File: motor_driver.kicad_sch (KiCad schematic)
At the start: 30 parts, among them J1 Motor_1_Conn, J11 Motor_2_Conn, J12 Motor_4_Conn, J14 Motor_5_Conn, J4 Motor_3_Conn, Q1 NMOS, Q2 NMOS, Q3 NMOS, Q4 NMOS, Q5 NMOS

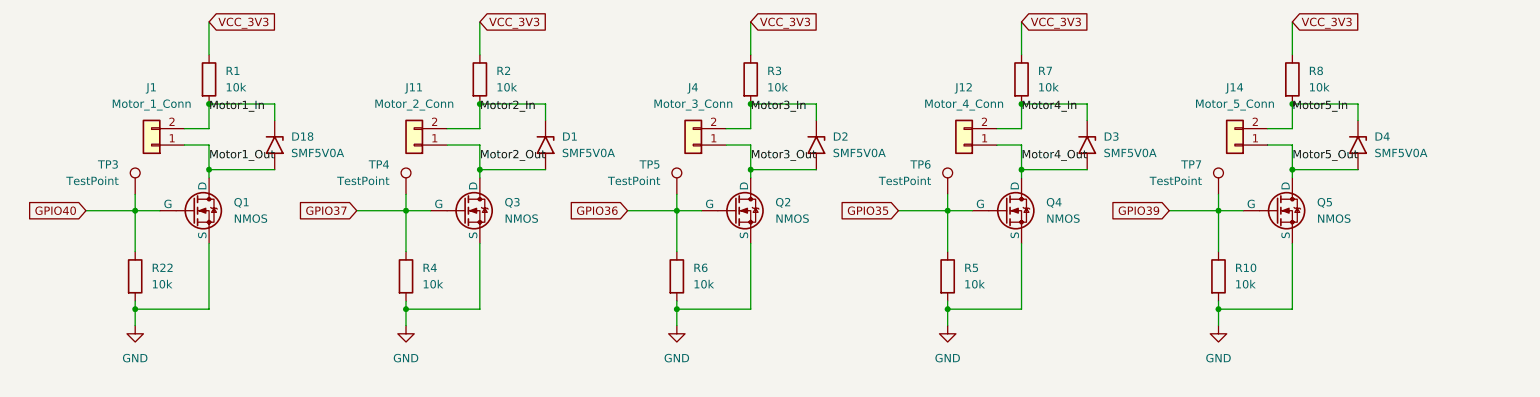
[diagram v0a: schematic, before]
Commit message: after connor fixed footprints and billy started layout
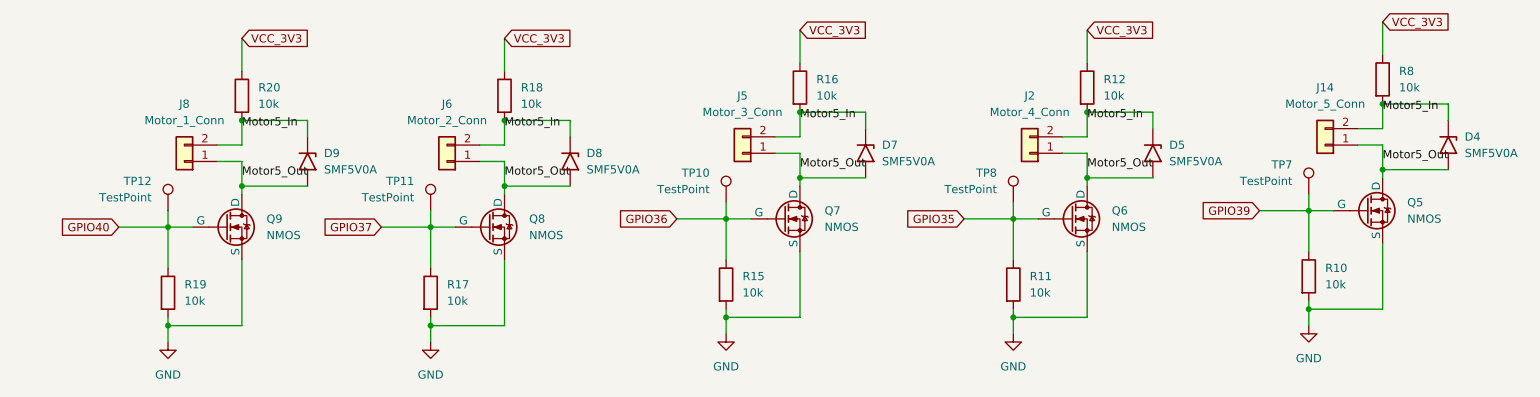
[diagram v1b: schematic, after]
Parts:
- removed D1, D18, D2, D3: SMF5V0A, Diode_SMD:D_SMF, symbol Diode:SMF5V0A
- removed J1: Motor_1_Conn, Connector_JST:JST_XH_B2B-XH-AM_1x02_P2.50mm_Vertical, symbol Connector_Generic:Conn_01x02
- removed J11: Motor_2_Conn, Connector_JST:JST_XH_B2B-XH-AM_1x02_P2.50mm_Vertical, symbol Connector_Generic:Conn_01x02
- removed J12: Motor_4_Conn, Connector_JST:JST_XH_B2B-XH-AM_1x02_P2.50mm_Vertical, symbol Connector_Generic:Conn_01x02
- removed J4: Motor_3_Conn, Connector_JST:JST_XH_B2B-XH-AM_1x02_P2.50mm_Vertical, symbol Connector_Generic:Conn_01x02
- removed Q1, Q2, Q3, Q4: NMOS, CustomComponents:SOT95P280X125-3N, symbol Simulation_SPICE:NMOS
- removed R1, R2, R22, R3, R4, R5, R6, R7: 10k, CustomComponents:STA_RMCF0402_STP, symbol Device:R
- removed TP3, TP4, TP5, TP6: TestPoint, symbol Connector:TestPoint
- added D5, D7, D8, D9: SMF5V0A, Diode_SMD:D_SMF, symbol Diode:SMF5V0A
- added J2: Motor_4_Conn, Connector_JST:JST_XH_B2B-XH-AM_1x02_P2.50mm_Vertical, symbol Connector_Generic:Conn_01x02
- added J5: Motor_3_Conn, Connector_JST:JST_XH_B2B-XH-AM_1x02_P2.50mm_Vertical, symbol Connector_Generic:Conn_01x02
- added J6: Motor_2_Conn, Connector_JST:JST_XH_B2B-XH-AM_1x02_P2.50mm_Vertical, symbol Connector_Generic:Conn_01x02
- added J8: Motor_1_Conn, Connector_JST:JST_XH_B2B-XH-AM_1x02_P2.50mm_Vertical, symbol Connector_Generic:Conn_01x02
- added Q6, Q7, Q8, Q9: NMOS, LocalComponents:SOT95P280X125-3N, symbol Simulation_SPICE:NMOS
- added R11, R12, R15, R16, R17, R18, R19, R20: 10k, LocalComponents:STA_RMCF0402_STP, symbol Device:R
- added TP10, TP11, TP12, TP8: TestPoint, symbol Connector:TestPoint
- Q5: footprint CustomComponents:SOT95P280X125-3N -> LocalComponents:SOT95P280X125-3N
- R10, R8: footprint CustomComponents:STA_RMCF0402_STP -> LocalComponents:STA_RMCF0402_STP
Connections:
- net GND: now also Q6.3 (S), Q7.3 (S), Q8.3 (S), Q9.3 (S), R11.2, R15.2, R17.2, R19.2
- net GPIO35: now also Q6.2 (G), R11.1, TP8.1
- net GPIO36: now also Q7.2 (G), R15.1, TP10.1
- net GPIO37: now also Q8.2 (G), R17.1, TP11.1
- net GPIO40: now also Q9.2 (G), R19.1, TP12.1
- net Motor5_In: now also D5.1 (A1), D7.1 (A1), D8.1 (A1), D9.1 (A1), J2.2 (Pin_2), J5.2 (Pin_2), J6.2 (Pin_2), J8.2 (Pin_2), R12.2, R16.2, R18.2, R20.2
- net Motor5_Out: now also D5.2 (A2), D7.2 (A2), D8.2 (A2), D9.2 (A2), J2.1 (Pin_1), J5.1 (Pin_1), J6.1 (Pin_1), J8.1 (Pin_1), Q6.1 (D), Q7.1 (D), Q8.1 (D), Q9.1 (D)
- net VCC_3V3: now also R12.1, R16.1, R18.1, R20.1
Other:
- moved on the sheet: D4, J14, Q5, R10, R8, TP7

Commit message: pcb layout done, billy watching over us
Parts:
- TP10, TP11, TP12, TP7, TP8: footprint (none) -> TestPoint:TestPoint_Pad_D1.5mm
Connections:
- removed net Motor5_In: D4.1 (A1), D5.1 (A1), D7.1 (A1), D8.1 (A1), D9.1 (A1), J14.2 (Pin_2), J2.2 (Pin_2), J5.2 (Pin_2), J6.2 (Pin_2), J8.2 (Pin_2), R12.2, R16.2, R18.2, R20.2, R8.2
- removed net Motor5_Out: D4.2 (A2), D5.2 (A2), D7.2 (A2), D8.2 (A2), D9.2 (A2), J14.1 (Pin_1), J2.1 (Pin_1), J5.1 (Pin_1), J6.1 (Pin_1), J8.1 (Pin_1), Q5.1 (D), Q6.1 (D), Q7.1 (D), Q8.1 (D), Q9.1 (D)
- new net Motor_1_in: D9.1 (A1), J8.2 (Pin_2), R20.2
- new net Motor_1_out: D9.2 (A2), J8.1 (Pin_1), Q9.1 (D)
- new net Motor_2_in: D8.1 (A1), J6.2 (Pin_2), R18.2
- new net Motor_2_out: D8.2 (A2), J6.1 (Pin_1), Q8.1 (D)
- new net Motor_3_in: D7.1 (A1), J5.2 (Pin_2), R16.2
- new net Motor_3_out: D7.2 (A2), J5.1 (Pin_1), Q7.1 (D)
- new net Motor_4_in: D5.1 (A1), J2.2 (Pin_2), R12.2
- new net Motor_4_out: D5.2 (A2), J2.1 (Pin_1), Q6.1 (D)
- new net Motor_5_in: D4.1 (A1), J14.2 (Pin_2), R8.2
- new net Motor_5_out: D4.2 (A2), J14.1 (Pin_1), Q5.1 (D)
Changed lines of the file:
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@@
 		)
 	)
-	(label "Motor5_In"
+	(label "Motor_1_in"
 		(at 40.64 31.75 0)
 		(effects
@@
 		)
 	)
-	(label "Motor5_In"
+	(label "Motor_3_in"
 		(at 127 30.48 0)
 		(effects
@@
 		)
 	)
-	(label "Motor5_In"
+	(label "Motor_4_in"
 		(at 171.45 30.48 0)
 		(effects
@@
 		)
 	)
-	(label "Motor5_Out"
+	(label "Motor_4_out"
 		(at 171.45 38.1 0)
 		(effects
@@
 		)
 	)
-	(label "Motor5_Out"
+	(label "Motor_1_out"
 		(at 40.64 39.37 0)
 		(effects
@@
 		)
 	)
-	(label "Motor5_Out"
+	(label "Motor_5_out"
 		(at 217.17 36.83 0)
 		(effects
@@
 		)
 	)
-	(label "Motor5_In"
+	(label "Motor_2_in"
 		(at 81.28 31.75 0)
 		(effects
@@
 		)
 	)
-	(label "Motor5_Out"
+	(label "Motor_3_out"
 		(at 127 38.1 0)
 		(effects
@@
 		)
 	)
-	(label "Motor5_In"
+	(label "Motor_5_in"
 		(at 217.17 29.21 0)
 		(effects
@@
 		)
 	)
-	(label "Motor5_Out"
+	(label "Motor_2_out"
 		(at 81.28 39.37 0)
 		(effects
@@
 			)
 		)
-		(property "Footprint" ""
+		(property "Footprint" "TestPoint:TestPoint_Pad_D1.5mm"
 			(at 154.94 43.18 0)
 			(effects
@@
 			)
 		)
-		(property "Footprint" ""
+		(property "Footprint" "TestPoint:TestPoint_Pad_D1.5mm"
 			(at 200.66 41.91 0)
 			(effects
@@
 			)
 		)
-		(property "Footprint" ""
+		(property "Footprint" "TestPoint:TestPoint_Pad_D1.5mm"
 			(at 64.77 44.45 0)
 			(effects
@@
 			)
 		)
-		(property "Footprint" ""
+		(property "Footprint" "TestPoint:TestPoint_Pad_D1.5mm"
 			(at 110.49 43.18 0)
 			(effects
@@
 			)
 		)
-		(property "Footprint" ""
+		(property "Footprint" "TestPoint:TestPoint_Pad_D1.5mm"
 			(at 24.13 44.45 0)
 			(effects

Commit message: pcb draft 2 from billy
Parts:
- R10, R11, R12, R15, R16, R17, R18, R19, R20, R8: footprint LocalComponents:STA_RMCF0402_STP -> Resistor_SMD:R_0805_2012Metric_Pad1.20x1.40mm_HandSolder
- TP10, TP11, TP12, TP7, TP8: footprint TestPoint:TestPoint_Pad_D1.5mm -> TestPoint_Pad_D1.0mm
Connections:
- net Motor_1_in renamed Motor1_In
- net Motor_1_out renamed Motor1_Out
- net Motor_2_in renamed Motor2_In
- net Motor_2_out renamed Motor2_Out
- net Motor_3_in renamed Motor3_In
- net Motor_3_out renamed Motor3_Out
- net Motor_4_in renamed Motor4_In
- net Motor_4_out renamed Motor4_Out
- net Motor_5_in renamed Motor5_In
- net Motor_5_out renamed Motor5_Out
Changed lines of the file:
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@@
 		)
 	)
-	(label "Motor_1_in"
+	(label "Motor1_In"
 		(at 40.64 31.75 0)
 		(effects
@@
 		)
 	)
-	(label "Motor_3_in"
+	(label "Motor3_In"
 		(at 127 30.48 0)
 		(effects
@@
 		)
 	)
-	(label "Motor_4_in"
+	(label "Motor4_In"
 		(at 171.45 30.48 0)
 		(effects
@@
 		)
 	)
-	(label "Motor_4_out"
+	(label "Motor4_Out"
 		(at 171.45 38.1 0)
 		(effects
@@
 		)
 	)
-	(label "Motor_1_out"
+	(label "Motor1_Out"
 		(at 40.64 39.37 0)
 		(effects
@@
 		)
 	)
-	(label "Motor_5_out"
+	(label "Motor5_Out"
 		(at 217.17 36.83 0)
 		(effects
@@
 		)
 	)
-	(label "Motor_2_in"
+	(label "Motor2_In"
 		(at 81.28 31.75 0)
 		(effects
@@
 		)
 	)
-	(label "Motor_3_out"
+	(label "Motor3_Out"
 		(at 127 38.1 0)
 		(effects
@@
 		)
 	)
-	(label "Motor_5_in"
+	(label "Motor5_In"
 		(at 217.17 29.21 0)
 		(effects
@@
 		)
 	)
-	(label "Motor_2_out"
+	(label "Motor2_Out"
 		(at 81.28 39.37 0)
 		(effects
@@
 			)
 		)
-		(property "Footprint" "LocalComponents:STA_RMCF0402_STP"
+		(property "Footprint" "Resistor_SMD:R_0805_2012Metric_Pad1.20x1.40mm_HandSolder"
 			(at 68.072 57.15 90)
 			(effects
@@
 			)
 		)
-		(property "Footprint" "TestPoint:TestPoint_Pad_D1.5mm"
+		(property "Footprint" "TestPoint_Pad_D1.0mm"
 			(at 154.94 43.18 0)
 			(effects
@@
 			)
 		)
-		(property "Footprint" "LocalComponents:STA_RMCF0402_STP"
+		(property "Footprint" "Resistor_SMD:R_0805_2012Metric_Pad1.20x1.40mm_HandSolder"
 			(at 27.432 57.15 90)
 			(effects
@@
 			)
 		)
-		(property "Footprint" "LocalComponents:STA_RMCF0402_STP"
+		(property "Footprint" "Resistor_SMD:R_0805_2012Metric_Pad1.20x1.40mm_HandSolder"
 			(at 169.672 25.4 90)
 			(effects
@@
 			)
 		)
-		(property "Footprint" "LocalComponents:STA_RMCF0402_STP"
+		(property "Footprint" "Resistor_SMD:R_0805_2012Metric_Pad1.20x1.40mm_HandSolder"
 			(at 215.392 24.13 90)
 			(effects
@@
 			)
 		)
-		(property "Footprint" "TestPoint:TestPoint_Pad_D1.5mm"
+		(property "Footprint" "TestPoint_Pad_D1.0mm"
 			(at 200.66 41.91 0)
 			(effects
@@
 			)
 		)
-		(property "Footprint" "TestPoint:TestPoint_Pad_D1.5mm"
+		(property "Footprint" "TestPoint_Pad_D1.0mm"
 			(at 64.77 44.45 0)
 			(effects
@@
 			)
 		)
-		(property "Footprint" "TestPoint:TestPoint_Pad_D1.5mm"
+		(property "Footprint" "TestPoint_Pad_D1.0mm"
 			(at 110.49 43.18 0)
 			(effects
@@
 			)
 		)
-		(property "Footprint" "LocalComponents:STA_RMCF0402_STP"
+		(property "Footprint" "Resistor_SMD:R_0805_2012Metric_Pad1.20x1.40mm_HandSolder"
 			(at 203.962 54.61 90)
 			(effects
@@
 			)
 		)
-		(property "Footprint" "LocalComponents:STA_RMCF0402_STP"
+		(property "Footprint" "Resistor_SMD:R_0805_2012Metric_Pad1.20x1.40mm_HandSolder"
 			(at 38.862 26.67 90)
 			(effects
@@
 			)
 		)
-		(property "Footprint" "TestPoint:TestPoint_Pad_D1.5mm"
+		(property "Footprint" "TestPoint_Pad_D1.0mm"
 			(at 24.13 44.45 0)
 			(effects
@@
 			)
 		)
-		(property "Footprint" "LocalComponents:STA_RMCF0402_STP"
+		(property "Footprint" "Resistor_SMD:R_0805_2012Metric_Pad1.20x1.40mm_HandSolder"
 			(at 113.792 55.88 90)
 			(effects
@@
 			)
 		)
-		(property "Footprint" "LocalComponents:STA_RMCF0402_STP"
+		(property "Footprint" "Resistor_SMD:R_0805_2012Metric_Pad1.20x1.40mm_HandSolder"
 			(at 79.502 26.67 90)
 			(effects
@@
 			)
 		)
-		(property "Footprint" "LocalComponents:STA_RMCF0402_STP"
+		(property "Footprint" "Resistor_SMD:R_0805_2012Metric_Pad1.20x1.40mm_HandSolder"
 			(at 125.222 25.4 90)
 			(effects
@@
 			)
 		)
-		(property "Footprint" "LocalComponents:STA_RMCF0402_STP"
+		(property "Footprint" "Resistor_SMD:R_0805_2012Metric_Pad1.20x1.40mm_HandSolder"
 			(at 158.242 55.88 90)
 			(effects
